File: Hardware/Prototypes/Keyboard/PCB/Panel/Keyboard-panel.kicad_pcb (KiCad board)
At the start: 4 copper layers, 66 x 45 mm, 112 parts, among them P1 USB_OTG, SW1 RESET, U1 ATMEGA32U4-QFN44, X1 ABM10-16.000MHZ-D30-T3

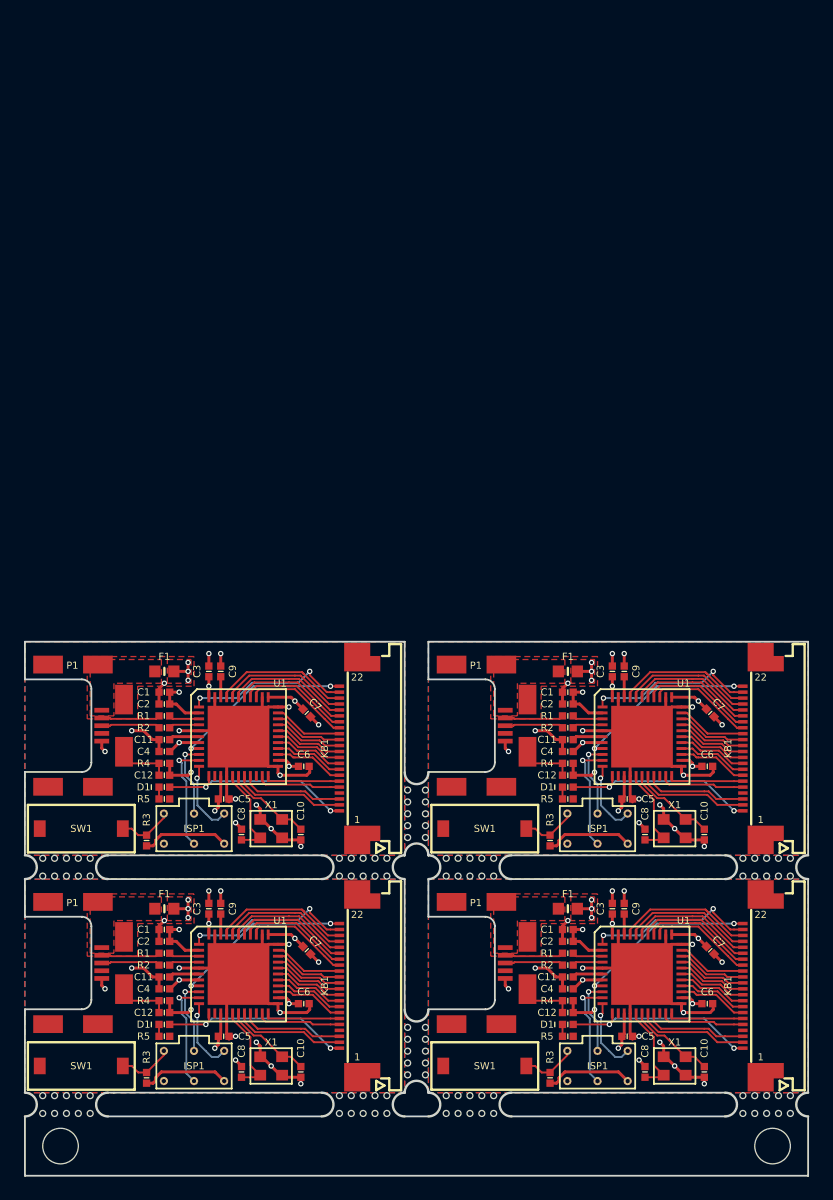
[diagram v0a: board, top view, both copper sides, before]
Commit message: Reverted to 2-layer board
Because it fits and is cheaper
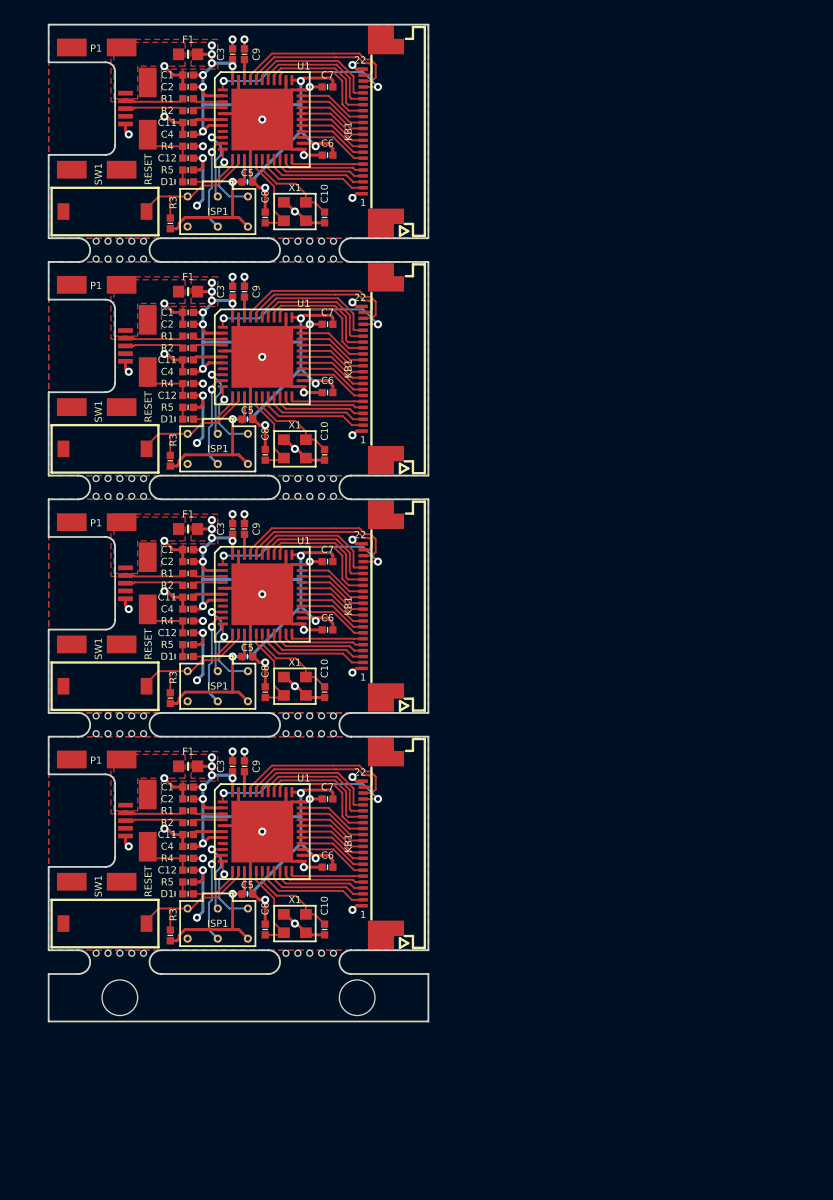
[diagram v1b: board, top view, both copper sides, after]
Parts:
- removed the C1 at (165.8, 110.2)
- removed the C1 at (131.8, 110.2)
- removed the C1 at (165.8, 90.2)
- removed the C10 at (177.2, 122.2)
- removed the C10 at (143.2, 122.2)
- removed the C10 at (177.2, 102.2)
- removed the C11 at (165.8, 114.2)
- removed the C11 at (131.8, 114.2)
- removed the C11 at (165.8, 94.2)
- removed the C12 at (165.8, 117.2)
- removed the C12 at (131.8, 117.2)
- removed the C12 at (165.8, 97.2)
- removed the C2 at (165.8, 111.2)
- removed the C2 at (131.8, 111.2)
- removed the C2 at (165.8, 91.2)
- removed the C3 at (169.5, 108.5)
- removed the C3 at (135.5, 108.5)
- removed the C3 at (169.5, 88.5)
- removed the C4 at (165.8, 115.2)
- removed the C4 at (131.8, 115.2)
- removed the C4 at (165.8, 95.2)
- removed the C5 at (170.8, 119.2)
- removed the C5 at (136.8, 119.2)
- removed the C5 at (170.8, 99.2)
- removed the C6 at (177.5, 116.5)
- removed the C6 at (143.5, 116.5)
- removed the C6 at (177.5, 96.5)
- removed the C7 at (177.8, 112.0)
- removed the C7 at (143.8, 112.0)
- removed the C7 at (177.8, 92.0)
- removed the C8 at (172.2, 122.2)
- removed the C8 at (138.2, 122.2)
- removed the C8 at (172.2, 102.2)
- removed the C9 at (170.5, 108.5)
- removed the C9 at (136.5, 108.5)
- removed the C9 at (170.5, 88.5)
- removed the D1 at (165.8, 118.2)
- removed the D1 at (131.8, 118.2)
- removed the D1 at (165.8, 98.2)
- removed the F1 at (165.8, 108.5)
- removed the F1 at (131.8, 108.5)
- removed the F1 at (165.8, 88.5)
- removed the ISP1 at (168.2, 121.8)
- removed the ISP1 at (134.2, 121.8)
- removed the ISP1 at (168.2, 101.8)
- removed the KB1 at (180.5, 115.0)
- removed the KB1 at (146.5, 115.0)
- removed the KB1 at (180.5, 95.0)
- removed the P1 at (154.0, 113.1)
- removed the P1 at (120.0, 113.1)
- removed the P1 at (154.0, 93.1)
- removed the R1 at (165.8, 112.2)
- removed the R1 at (131.8, 112.2)
- removed the R1 at (165.8, 92.2)
- removed the R2 at (165.8, 113.2)
- removed the R2 at (131.8, 113.2)
- removed the R2 at (165.8, 93.2)
- removed the R3 at (164.2, 122.8)
- removed the R3 at (130.2, 122.8)
- removed the R3 at (164.2, 102.8)
- removed the R4 at (165.8, 116.2)
- removed the R4 at (131.8, 116.2)
- removed the R4 at (165.8, 96.2)
- removed the R5 at (165.8, 119.2)
- removed the R5 at (131.8, 119.2)
- removed the R5 at (165.8, 99.2)
- removed the REF** at (153.0, 120.5)
- removed the REF** at (123.5, 125.0)
- removed the REF** at (153.0, 100.5)
- removed the REF** at (123.5, 105.0)
- removed the REF** at (148.5, 105.0)
- removed the REF** at (157.5, 105.0)
- removed the REF** at (182.5, 105.0)
- removed the REF** at (182.5, 125.0)
- removed the REF** at (157.5, 125.0)
- removed the REF** at (148.5, 125.0)
- removed the SW1 at (158.8, 121.8)
- removed the SW1 at (124.8, 121.8)
- removed the SW1 at (158.8, 101.8)
- removed the U1 at (172.0, 114.0)
- removed the U1 at (138.0, 114.0)
- removed the U1 at (172.0, 94.0)
- removed the X1 at (174.8, 121.8)
- removed the X1 at (140.8, 121.8)
- removed the X1 at (174.8, 101.8)
- added C1: 1µ, SMD-DiscreteB:C-0402-1005, F.Cu at (133.8, 98.2)
- added C1: 1µ, SMD-DiscreteB:C-0402-1005, F.Cu at (133.8, 78.2)
- added C1: 1µ, SMD-DiscreteB:C-0402-1005, F.Cu at (133.8, 58.2)
- added C10: 15p, SMD-DiscreteB:C-0402-1005, F.Cu at (145.2, 110.2)
- added C10: 15p, SMD-DiscreteB:C-0402-1005, F.Cu at (145.2, 90.2)
- added C10: 15p, SMD-DiscreteB:C-0402-1005, F.Cu at (145.2, 70.2)
- added C11: 1µ, SMD-DiscreteB:C-0402-1005, F.Cu at (133.8, 102.2)
- added C11: 1µ, SMD-DiscreteB:C-0402-1005, F.Cu at (133.8, 82.2)
- added C11: 1µ, SMD-DiscreteB:C-0402-1005, F.Cu at (133.8, 62.2)
- added C12: 4n7, SMD-DiscreteB:C-0402-1005, F.Cu at (133.8, 105.2)
- added C12: 4n7, SMD-DiscreteB:C-0402-1005, F.Cu at (133.8, 85.2)
- added C12: 4n7, SMD-DiscreteB:C-0402-1005, F.Cu at (133.8, 65.2)
- added C2: 100n, SMD-DiscreteB:C-0402-1005, F.Cu at (133.8, 99.2)
- added C2: 100n, SMD-DiscreteB:C-0402-1005, F.Cu at (133.8, 79.2)
- added C2: 100n, SMD-DiscreteB:C-0402-1005, F.Cu at (133.8, 59.2)
- added C3: 100n, SMD-DiscreteB:C-0402-1005, F.Cu at (137.5, 96.5)
- added C3: 100n, SMD-DiscreteB:C-0402-1005, F.Cu at (137.5, 76.5)
- added C3: 100n, SMD-DiscreteB:C-0402-1005, F.Cu at (137.5, 56.5)
- added C4: 100n, SMD-DiscreteB:C-0402-1005, F.Cu at (133.8, 103.2)
- added C4: 100n, SMD-DiscreteB:C-0402-1005, F.Cu at (133.8, 83.2)
- added C4: 100n, SMD-DiscreteB:C-0402-1005, F.Cu at (133.8, 63.2)
- added C5: 100n, SMD-DiscreteB:C-0402-1005, F.Cu at (138.8, 107.2)
- added C5: 100n, SMD-DiscreteB:C-0402-1005, F.Cu at (138.8, 87.2)
- added C5: 100n, SMD-DiscreteB:C-0402-1005, F.Cu at (138.8, 67.2)
- added C6: 100n, SMD-DiscreteB:C-0402-1005, F.Cu at (145.5, 105.0)
- added C6: 100n, SMD-DiscreteB:C-0402-1005, F.Cu at (145.5, 85.0)
- added C6: 100n, SMD-DiscreteB:C-0402-1005, F.Cu at (145.5, 65.0)
- added C7: 100n, SMD-DiscreteB:C-0402-1005, F.Cu at (145.5, 99.2)
- added C7: 100n, SMD-DiscreteB:C-0402-1005, F.Cu at (145.5, 79.2)
- added C7: 100n, SMD-DiscreteB:C-0402-1005, F.Cu at (145.5, 59.2)
- added C8: 15p, SMD-DiscreteB:C-0402-1005, F.Cu at (140.2, 110.2)
- added C8: 15p, SMD-DiscreteB:C-0402-1005, F.Cu at (140.2, 90.2)
- added C8: 15p, SMD-DiscreteB:C-0402-1005, F.Cu at (140.2, 70.2)
- added C9: 100n, SMD-DiscreteB:C-0402-1005, F.Cu at (138.5, 96.5)
- added C9: 100n, SMD-DiscreteB:C-0402-1005, F.Cu at (138.5, 76.5)
- added C9: 100n, SMD-DiscreteB:C-0402-1005, F.Cu at (138.5, 56.5)
- added D1: STATUS, SMD-DiscreteB:LED-0402-1005, F.Cu at (133.8, 107.2)
- added D1: STATUS, SMD-DiscreteB:LED-0402-1005, F.Cu at (133.8, 87.2)
- added D1: STATUS, SMD-DiscreteB:LED-0402-1005, F.Cu at (133.8, 67.2)
- added F1: 500mA, SMD-DiscreteB:F-0603-1608, F.Cu at (133.8, 96.5)
- added F1: 500mA, SMD-DiscreteB:F-0603-1608, F.Cu at (133.8, 76.5)
- added F1: 500mA, SMD-DiscreteB:F-0603-1608, F.Cu at (133.8, 56.5)
- added ISP1: ATMEL_ISP-6P, SMD-Connectors:ISP-PADS_2mm54, F.Cu at (136.2, 109.8)
- added ISP1: ATMEL_ISP-6P, SMD-Connectors:ISP-PADS_2mm54, F.Cu at (136.2, 89.8)
- added ISP1: ATMEL_ISP-6P, SMD-Connectors:ISP-PADS_2mm54, F.Cu at (136.2, 69.8)
- added KB1: KEYBOARD-PSION-5MX, SMD-Connectors:FPC_0.5mm_22p-MOLEX_52437, F.Cu at (148.5, 103.0)
- added KB1: KEYBOARD-PSION-5MX, SMD-Connectors:FPC_0.5mm_22p-MOLEX_52437, F.Cu at (148.5, 83.0)
- added KB1: KEYBOARD-PSION-5MX, SMD-Connectors:FPC_0.5mm_22p-MOLEX_52437, F.Cu at (148.5, 63.0)
- added P1: USB_OTG, SMD-Connectors:USB-MICRO-MOLEX-47491-0001, F.Cu at (122.0, 101.1)
- added P1: USB_OTG, SMD-Connectors:USB-MICRO-MOLEX-47491-0001, F.Cu at (122.0, 81.1)
- added P1: USB_OTG, SMD-Connectors:USB-MICRO-MOLEX-47491-0001, F.Cu at (122.0, 61.1)
- added R1: 22, SMD-DiscreteB:R-0402-1005, F.Cu at (133.8, 100.2)
- added R1: 22, SMD-DiscreteB:R-0402-1005, F.Cu at (133.8, 80.2)
- added R1: 22, SMD-DiscreteB:R-0402-1005, F.Cu at (133.8, 60.2)
- added R2: 22, SMD-DiscreteB:R-0402-1005, F.Cu at (133.8, 101.2)
- added R2: 22, SMD-DiscreteB:R-0402-1005, F.Cu at (133.8, 81.2)
- added R2: 22, SMD-DiscreteB:R-0402-1005, F.Cu at (133.8, 61.2)
- added R3: 10k, SMD-DiscreteB:R-0402-1005, F.Cu at (132.2, 110.8)
- added R3: 10k, SMD-DiscreteB:R-0402-1005, F.Cu at (132.2, 90.8)
- added R3: 10k, SMD-DiscreteB:R-0402-1005, F.Cu at (132.2, 70.8)
- added R4: 1M, SMD-DiscreteB:R-0402-1005, F.Cu at (133.8, 104.2)
- added R4: 1M, SMD-DiscreteB:R-0402-1005, F.Cu at (133.8, 84.2)
- added R4: 1M, SMD-DiscreteB:R-0402-1005, F.Cu at (133.8, 64.2)
- added R5: 1k, SMD-DiscreteB:R-0402-1005, F.Cu at (133.8, 106.2)
- added R5: 1k, SMD-DiscreteB:R-0402-1005, F.Cu at (133.8, 86.2)
- added R5: 1k, SMD-DiscreteB:R-0402-1005, F.Cu at (133.8, 66.2)
- added REF**: MOUSEBITE_DOUBLE_2x5mm, Mechanical:MOUSEBITE_DOUBLE_OUTER_2x5mm, F.Cu at (144.0, 93.0)
- added REF**: MOUSEBITE_2x5mm, Mechanical:MOUSEBITE_OUTER_2x5mm, F.Cu at (144.0, 112.0)
- added REF**: MOUSEBITE_DOUBLE_2x5mm, Mechanical:MOUSEBITE_DOUBLE_OUTER_2x5mm, F.Cu at (144.0, 73.0)
- added REF**: MOUSEBITE_DOUBLE_2x5mm, Mechanical:MOUSEBITE_DOUBLE_OUTER_2x5mm, F.Cu at (128.0, 93.0)
- added REF**: MOUSEBITE_DOUBLE_2x5mm, Mechanical:MOUSEBITE_DOUBLE_OUTER_2x5mm, F.Cu at (128.0, 73.0)
- added REF**: MOUSEBITE_DOUBLE_2x5mm, Mechanical:MOUSEBITE_DOUBLE_OUTER_2x5mm, F.Cu at (128.0, 53.0)
- added REF**: MOUSEBITE_DOUBLE_2x5mm, Mechanical:MOUSEBITE_DOUBLE_OUTER_2x5mm, F.Cu at (144.0, 53.0)
- added REF**: MOUSEBITE_2x5mm, Mechanical:MOUSEBITE_OUTER_2x5mm, F.Cu at (128.0, 112.0)
- added SW1: RESET, SMD-Switches:KSR251GLFS, F.Cu at (126.8, 109.8)
- added SW1: RESET, SMD-Switches:KSR251GLFS, F.Cu at (126.8, 89.8)
- added SW1: RESET, SMD-Switches:KSR251GLFS, F.Cu at (126.8, 69.8)
- added U1: ATMEGA32U4-QFN44, SMD-QFN:VQFN-44_ATMEL, F.Cu at (140.0, 102.0)
- added U1: ATMEGA32U4-QFN44, SMD-QFN:VQFN-44_ATMEL, F.Cu at (140.0, 82.0)
- added U1: ATMEGA32U4-QFN44, SMD-QFN:VQFN-44_ATMEL, F.Cu at (140.0, 62.0)
- added X1: ABM10-16.000MHZ-D30-T3, SMD-XTAL:2.5x2mm, F.Cu at (142.8, 109.8)
- added X1: ABM10-16.000MHZ-D30-T3, SMD-XTAL:2.5x2mm, F.Cu at (142.8, 89.8)
- added X1: ABM10-16.000MHZ-D30-T3, SMD-XTAL:2.5x2mm, F.Cu at (142.8, 69.8)
- moved R5 53.0 mm to (133.8, 46.2)
- moved C7 52.8 mm to (145.5, 39.2), turned to 180 degrees
- moved C1 52.0 mm to (133.8, 38.2)
- moved C10 52.0 mm to (145.2, 50.2)
- moved C11 52.0 mm to (133.8, 42.2)
- moved C12 52.0 mm to (133.8, 45.2)
- moved C2 52.0 mm to (133.8, 39.2)
- moved C3 52.0 mm to (137.5, 36.5)
- moved C4 52.0 mm to (133.8, 43.2)
- moved C5 52.0 mm to (138.8, 47.2)
- moved C8 52.0 mm to (140.2, 50.2)
- moved C9 52.0 mm to (138.5, 36.5)
- moved F1 52.0 mm to (133.8, 36.5)
- moved ISP1 52.0 mm to (136.2, 49.8)
- moved KB1 52.0 mm to (148.5, 43.0)
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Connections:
- KB1 pad 1: /LED -> GND
- KB1 pad 22: /TMP -> GND
- U1 pad 1: /ROW_01 -> /ROW_07
- U1 pad 40: /ROW_07 -> /ROW_01
- U1 pad 8: /TMP -> (no net)
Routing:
- net +5V: track 112.2 -> 248.6 mm, vias 36 -> 40
- net /TMP: track 61.4 -> 0.00 mm, vias 8 -> 0
- net /LED: track 66.3 -> 17.5 mm, vias 8 -> 0
- net /COL_10: track 0.00 -> 31.7 mm
- net /RESET: track 18.6 -> 47.4 mm
- net /ROW_07: track 44.0 -> 63.4 mm, vias 0 -> 8
- net GND: track 213.2 -> 226.2 mm
- net /ROW_08: track 46.6 -> 57.5 mm
- net /ROW_01: track 57.5 -> 49.8 mm, vias 8 -> 0
- net /ROW_05: track 35.5 -> 41.8 mm
- net /MOSI: track 36.9 -> 41.6 mm
- net /COL_1: track 37.6 -> 42.3 mm
- net /ROW_02: track 39.7 -> 43.7 mm
- net /ROW_06: track 41.9 -> 45.2 mm
- net /COL_6: track 25.2 -> 23.6 mm
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- removed copper zone on Supply.Cu, net +5V
- removed copper zone on Ground.Cu, net GND
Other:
- board size 66 x 45 mm -> 32 x 84 mm
- copper layers 4 -> 2
- net class Default: clearance 0.127 -> 0.1524; via_dia 0.4572 -> 0.6858; via_drill 0.254 -> 0.3302
- net class Power: clearance 0.127 -> 0.1524; via_dia 0.4572 -> 0.6858; via_drill 0.254 -> 0.3302
- rule trace_clearance: 0.127 -> 0.1524
- rule via_min_drill: 0.254 -> 0.3302
- rule via_min_size: 0.4572 -> 0.6858
